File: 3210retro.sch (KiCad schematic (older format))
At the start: 11 parts, among them P101 USB_OTG, P102 LIPO, P103 DC, P104 NIMH, P105 EAR, P106 SPEAKER, P107 HEADPHONE, P109 RUMBLE, X101 ANT_GPS, X102 ANT_GSM

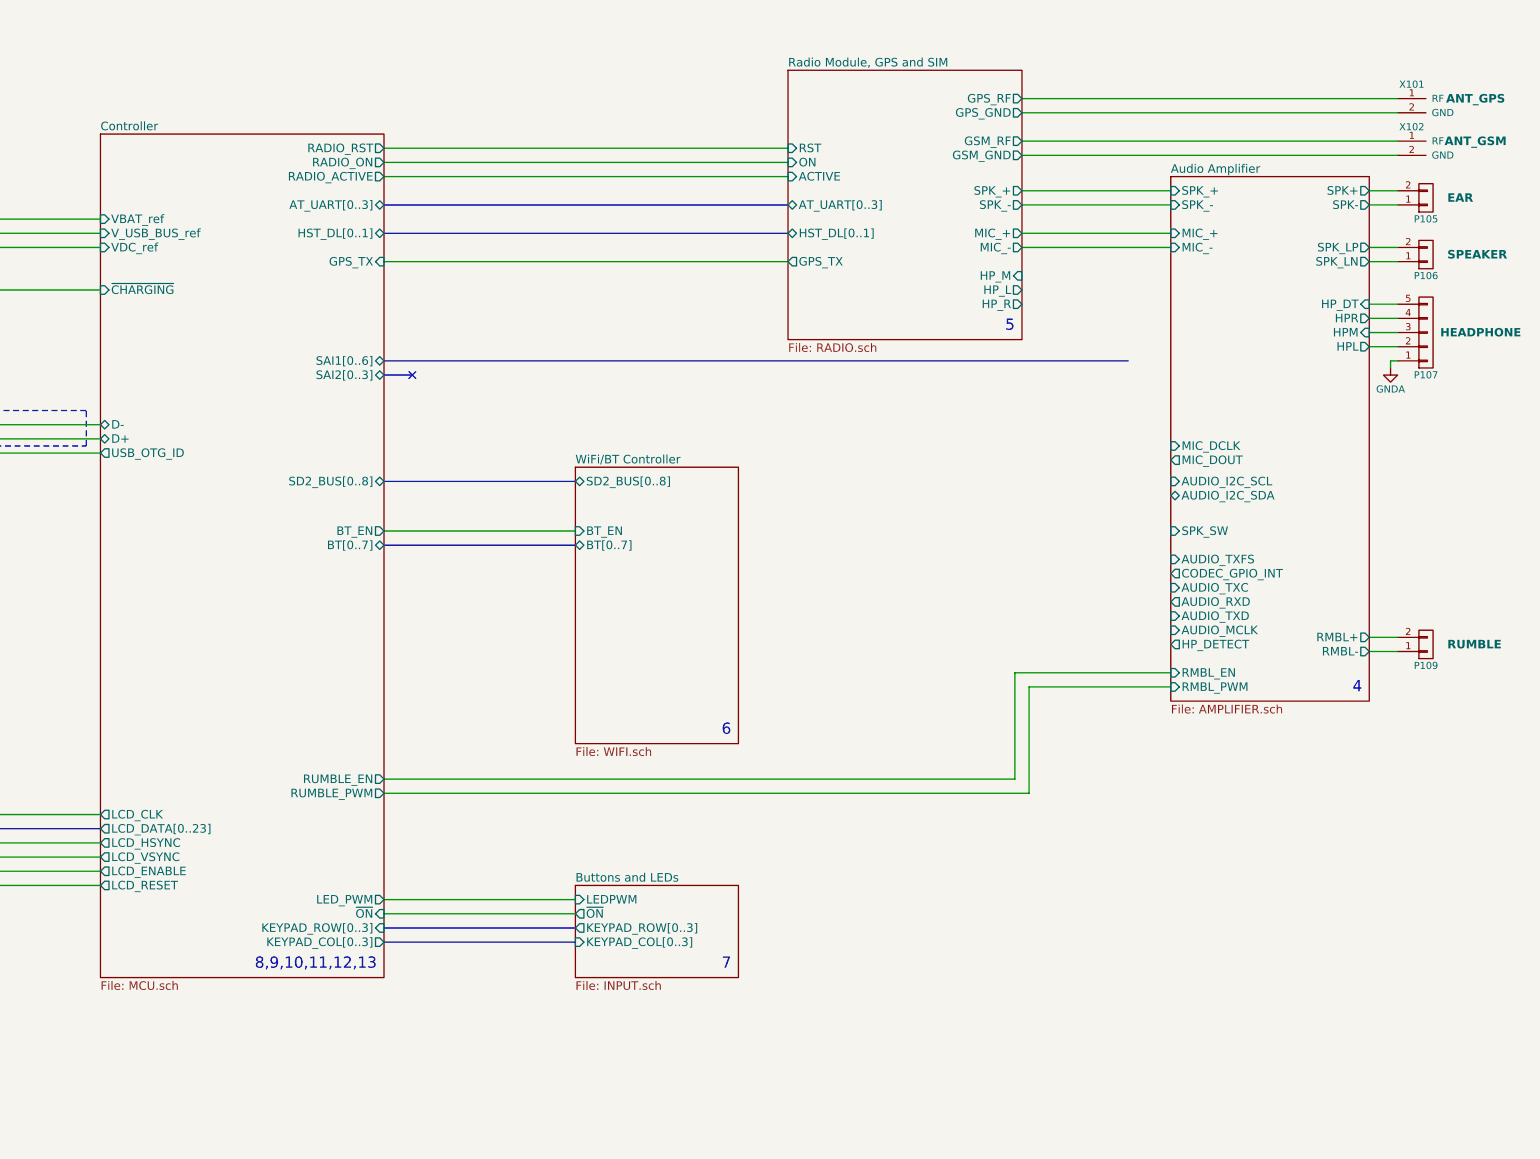
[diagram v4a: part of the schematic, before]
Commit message: on battery charging circuit for NiMH battery
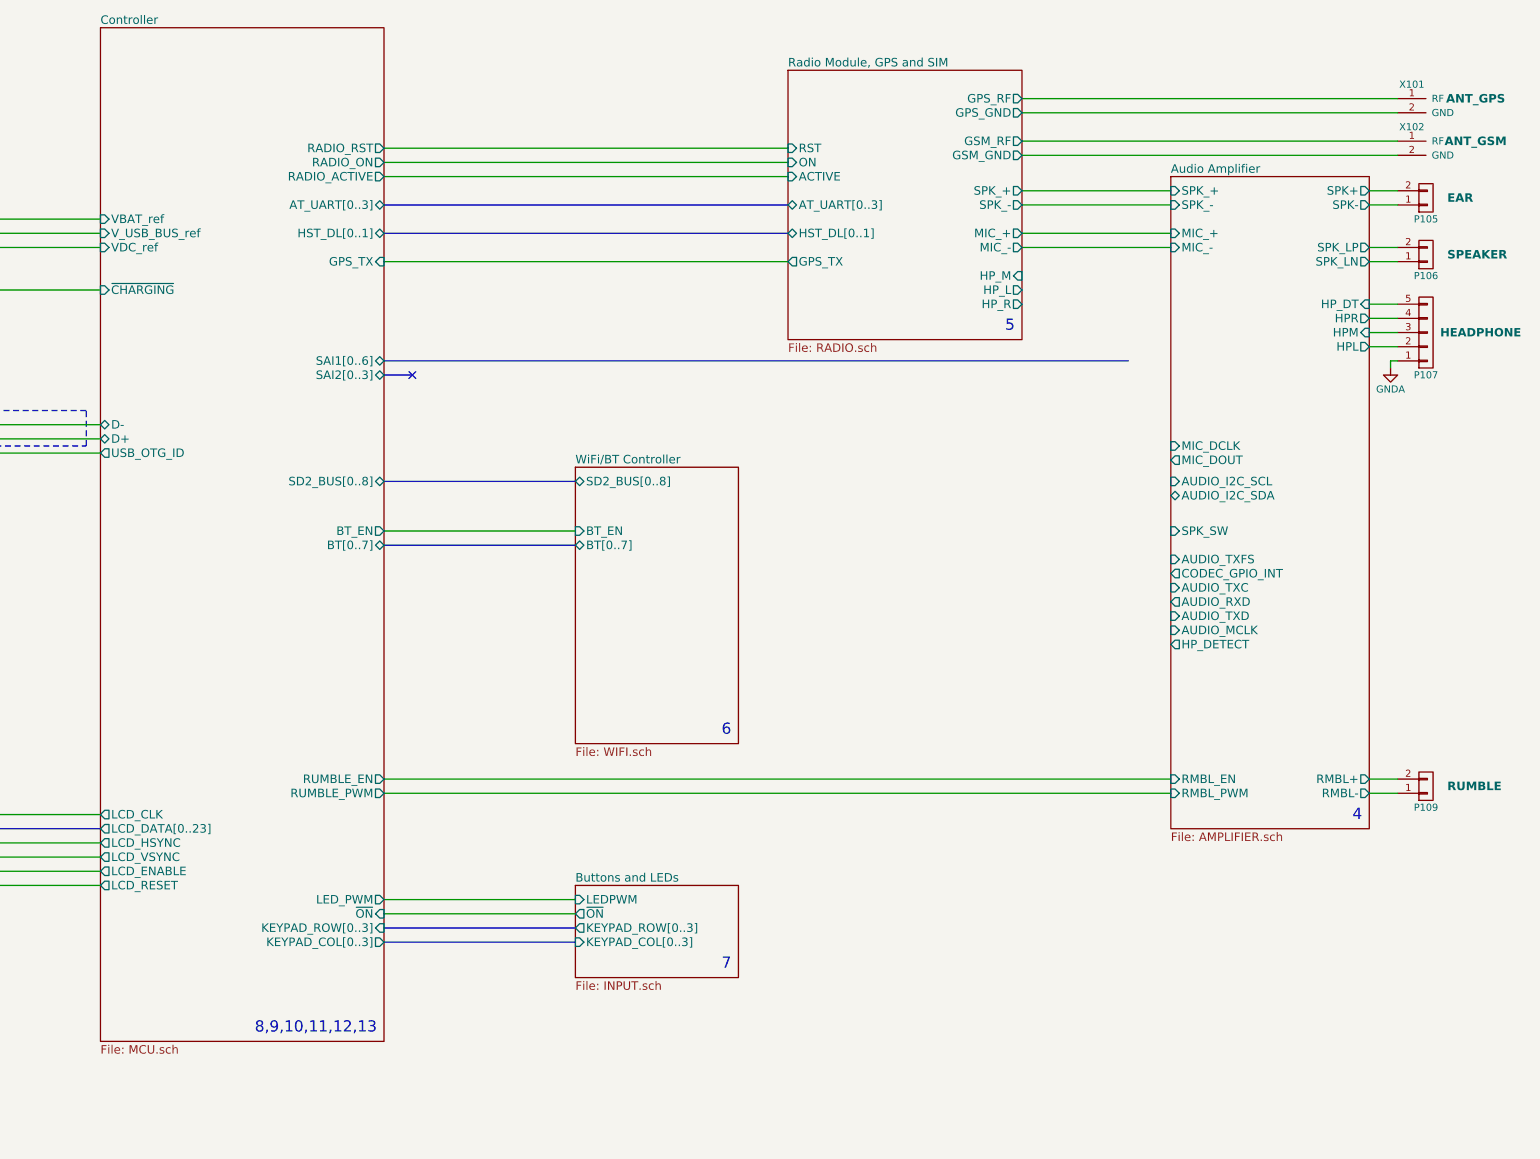
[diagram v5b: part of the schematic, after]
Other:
- moved on the sheet: P109
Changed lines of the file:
@@
 	1900 2900 2200 2900
 $Sheet
-S 13200 2600 1400 3700
+S 13200 2600 1400 4600
 U 5805F4B1
 F0 "Audio Amplifier" 60
@@
 F7 "HPL" O R 14600 3800 60
 F8 "HPR" O R 14600 3600 60
-F9 "RMBL+" O R 14600 5850 60
+F9 "RMBL+" O R 14600 6850 60
 F10 "MIC_DCLK" I L 13200 4500 60
 F11 "MIC_DOUT" O L 13200 4600 60
-F12 "RMBL-" O R 14600 5950 60
-F13 "RMBL_PWM" I L 13200 6200 60
-F14 "RMBL_EN" I L 13200 6100 60
+F12 "RMBL-" O R 14600 6950 60
+F13 "RMBL_PWM" I L 13200 6950 60
+F14 "RMBL_EN" I L 13200 6850 60
 F15 "SPK_SW" I L 13200 5100 60
 F16 "CODEC_GPIO_INT" O L 13200 5400 60
@@
 L CONN_01X02 P109
 U 1 1 580EBF81
-P 15000 5900
-F 0 "P109" H 15000 6050 50  0000 C CNN
-F 1 "RUMBLE" H 15150 5900 60  0000 L CNB
-F 2 "Pin_Headers:Pin_Header_Straight_1x02" H 15000 5900 50  0001 C CNN
-F 3 "" H 15000 5900 50  0000 C CNN
-	1    15000 5900
+P 15000 6900
+F 0 "P109" H 15000 7050 50  0000 C CNN
+F 1 "RUMBLE" H 15150 6900 60  0000 L CNB
+F 2 "Pin_Headers:Pin_Header_Straight_1x02" H 15000 6900 50  0001 C CNN
+F 3 "" H 15000 6900 50  0000 C CNN
+	1    15000 6900
 	1    0    0    1
 $EndComp
 Wire Wire Line
-	14600 5950 14800 5950
-Wire Wire Line
-	14600 5850 14800 5850
+	14600 6950 14800 6950
+Wire Wire Line
+	14600 6850 14800 6850
 $Sheet
 S 9000 7600 1150 650
@@
 	7650 7700 9000 7700
 Wire Wire Line
-	12200 6200 12200 6950
-Wire Wire Line
-	12200 6200 13200 6200
-Wire Wire Line
-	13200 6100 12100 6100
-Wire Wire Line
-	12100 6100 12100 6850
-Wire Wire Line
-	12100 6850 7650 6850
-Wire Wire Line
-	12200 6950 7650 6950
+	7650 6950 13200 6950
+Wire Wire Line
+	7650 6850 13200 6850
 $Comp
 L USB_OTG-RESCUE-3210retro P101
@@
 	14750 3900 14750 3950
 $Sheet
-S 5650 2300 2000 5950
+S 5650 1550 2000 7150
 U 5805F47D
 F0 "Controller" 60
@@
 Text Notes 2500 7850 2    79   ~ 0
 3
-Text Notes 14550 6250 2    79   ~ 0
+Text Notes 14550 7150 2    79   ~ 0
 4
 Text Notes 12100 3700 2    79   ~ 0
@@
 Text Notes 10100 8200 2    79   ~ 0
 7
-Text Notes 7600 8200 2    79   ~ 0
+Text Notes 7600 8650 2    79   ~ 0
 8,9,10,11,12,13
 $EndSCHEMATC

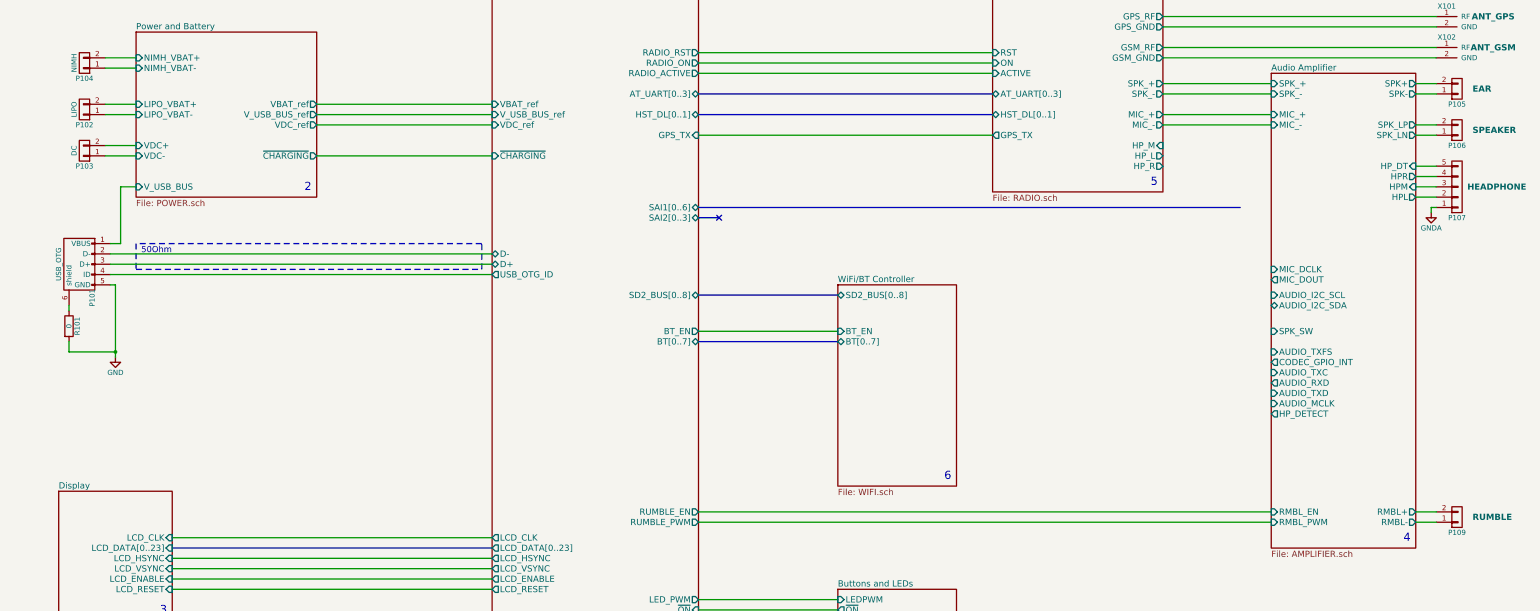
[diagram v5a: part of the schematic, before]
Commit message: Changed several voltage rail connections Removed non existing rails Added circuit for NiMH charging
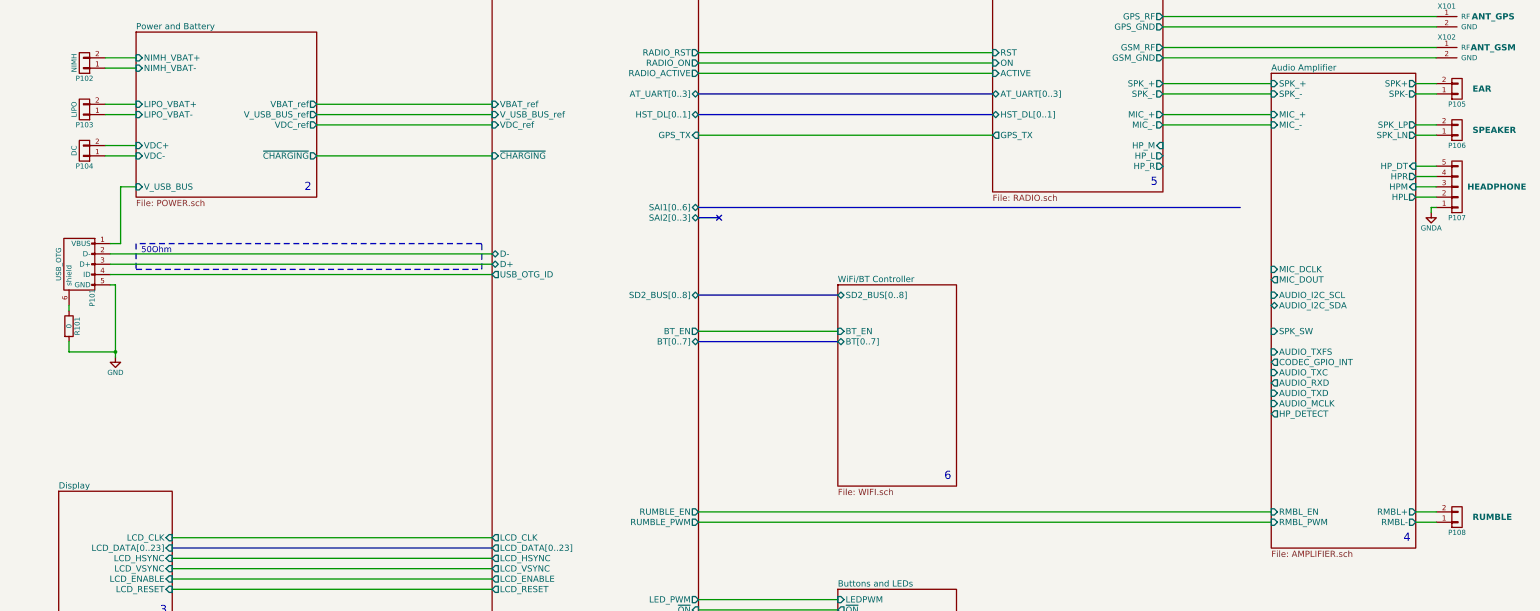
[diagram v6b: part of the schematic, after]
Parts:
- renumbered P104 to P102, P102 to P103, P103 to P104, P109 to P108
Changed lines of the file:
@@
 $EndSheet
 $Comp
-L CONN_01X02 P102
+L CONN_01X02 P103
 U 1 1 580667EA
 P 1700 2950
-F 0 "P102" H 1700 3100 50  0000 C CNN
+F 0 "P103" H 1700 3100 50  0000 C CNN
 F 1 "LIPO" V 1800 2950 50  0000 C CNN
 F 2 "Pin_Headers:Pin_Header_Straight_2x01" H 1700 2950 50  0001 C CNN
@@
 	14600 2800 14800 2800
 $Comp
-L GNDA #PWR102
+L GNDA #PWR01
 U 1 1 58075318
 P 14750 3950
-F 0 "#PWR102" H 14750 3700 50  0001 C CNN
+F 0 "#PWR01" H 14750 3700 50  0001 C CNN
 F 1 "GNDA" H 14750 3800 50  0000 C CNN
 F 2 "" H 14750 3950 50  0000 C CNN
@@
 	7650 2500 10500 2500
 $Comp
-L GND #PWR101
+L GND #PWR02
 U 1 1 580BB0C9
 P 2000 5350
-F 0 "#PWR101" H 2000 5100 50  0001 C CNN
+F 0 "#PWR02" H 2000 5100 50  0001 C CNN
 F 1 "GND" H 2000 5200 50  0000 C CNN
 F 2 "" H 2000 5350 50  0000 C CNN
@@
 	2050 3700 2200 3700
 $Comp
-L CONN_01X02 P103
+L CONN_01X02 P104
 U 1 1 580C5E12
 P 1700 3350
-F 0 "P103" H 1700 3500 50  0000 C CNN
+F 0 "P104" H 1700 3500 50  0000 C CNN
 F 1 "DC" V 1800 3350 50  0000 C CNN
 F 2 "Pin_Headers:Pin_Header_Straight_2x01" H 1700 3350 50  0001 C CNN
@@
 $EndSheet
 $Comp
-L CONN_01X02 P109
+L CONN_01X02 P108
 U 1 1 580EBF81
 P 15000 6900
-F 0 "P109" H 15000 7050 50  0000 C CNN
+F 0 "P108" H 15000 7050 50  0000 C CNN
 F 1 "RUMBLE" H 15150 6900 60  0000 L CNB
 F 2 "Pin_Headers:Pin_Header_Straight_1x02" H 15000 6900 50  0001 C CNN
@@
 	10500 2400 7650 2400
 $Comp
-L CONN_01X02 P104
+L CONN_01X02 P102
 U 1 1 5956D99A
 P 1700 2500
-F 0 "P104" H 1700 2650 50  0000 C CNN
+F 0 "P102" H 1700 2650 50  0000 C CNN
 F 1 "NIMH" V 1800 2500 50  0000 C CNN
 F 2 "Pin_Headers:Pin_Header_Straight_2x01" H 1700 2500 50  0001 C CNN

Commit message: Created netlist with current components Foreward Annotation to Board
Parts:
- P101: footprint (none) -> Connect:USB_Micro-B_10103594-0001LF
- P107: footprint (none) -> Pin_Headers:Pin_Header_Straight_1x05
- R101: footprint (none) -> Resistors_SMD:R_0402
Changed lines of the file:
@@
 F 0 "P101" H 1975 4325 50  0000 C CNN
 F 1 "USB_OTG" H 1650 4650 50  0000 C CNN
-F 2 "" V 1600 4350 50  0000 C CNN
+F 2 "Connect:USB_Micro-B_10103594-0001LF" V 1600 4350 50  0001 C CNN
 F 3 "" V 1600 4350 50  0000 C CNN
 	1    1650 4450
@@
 F 0 "R101" V 1630 5050 50  0000 C CNN
 F 1 "0" V 1550 5050 50  0000 C CNN
-F 2 "" V 1480 5050 50  0000 C CNN
+F 2 "Resistors_SMD:R_0402" V 1480 5050 50  0001 C CNN
 F 3 "" H 1550 5050 50  0000 C CNN
 	1    1550 5050
@@
 F 0 "P107" H 15000 4000 50  0000 C CNN
 F 1 "HEADPHONE" H 15100 3700 59  0000 L CNB
-F 2 "" H 15000 3700 50  0000 C CNN
+F 2 "Pin_Headers:Pin_Header_Straight_1x05" H 15000 3700 50  0001 C CNN
 F 3 "" H 15000 3700 50  0000 C CNN
 	1    15000 3700

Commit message: This branch moves from i.mx7 to STM32F4 CPU to be finished for Hackaday Prize 2017
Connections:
- net Controller/D+ renamed Controller/USB_DP
- net Controller/D- renamed Controller/USB_DM
- net Controller/USB_OTG_ID renamed Controller/USB_ID
- net Power and Battery/V_USB_BUS renamed Controller/USB_VBUS
- no-connect marks 1 -> 0
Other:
- note added: "50 Ohm"
- note added: "Display has its own I2C BUS"
- note added: "uSD-Card Slot"
- note removed: "50Ohm"
- moved on the sheet: P101, P102, P103, P104, R101
